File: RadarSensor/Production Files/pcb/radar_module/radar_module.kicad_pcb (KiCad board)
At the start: 2 copper layers, 50 x 25 mm, 14 parts, among them J1 110990030, J3 Conn_01x05_Pin, J4 Conn_02x04_Odd_Even, U1 MIC2288YD5-TR

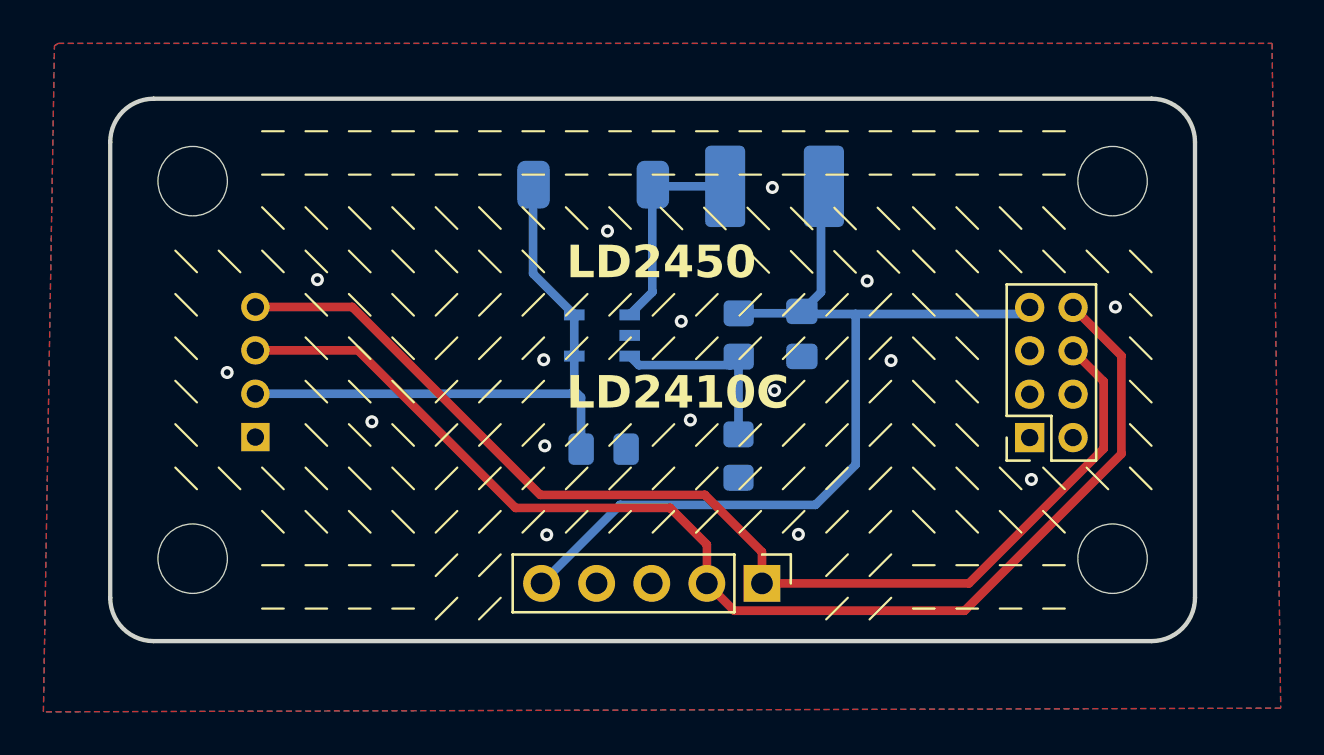
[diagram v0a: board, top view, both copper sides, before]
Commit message: silkscreen for radar sensor, more code examples, better readme
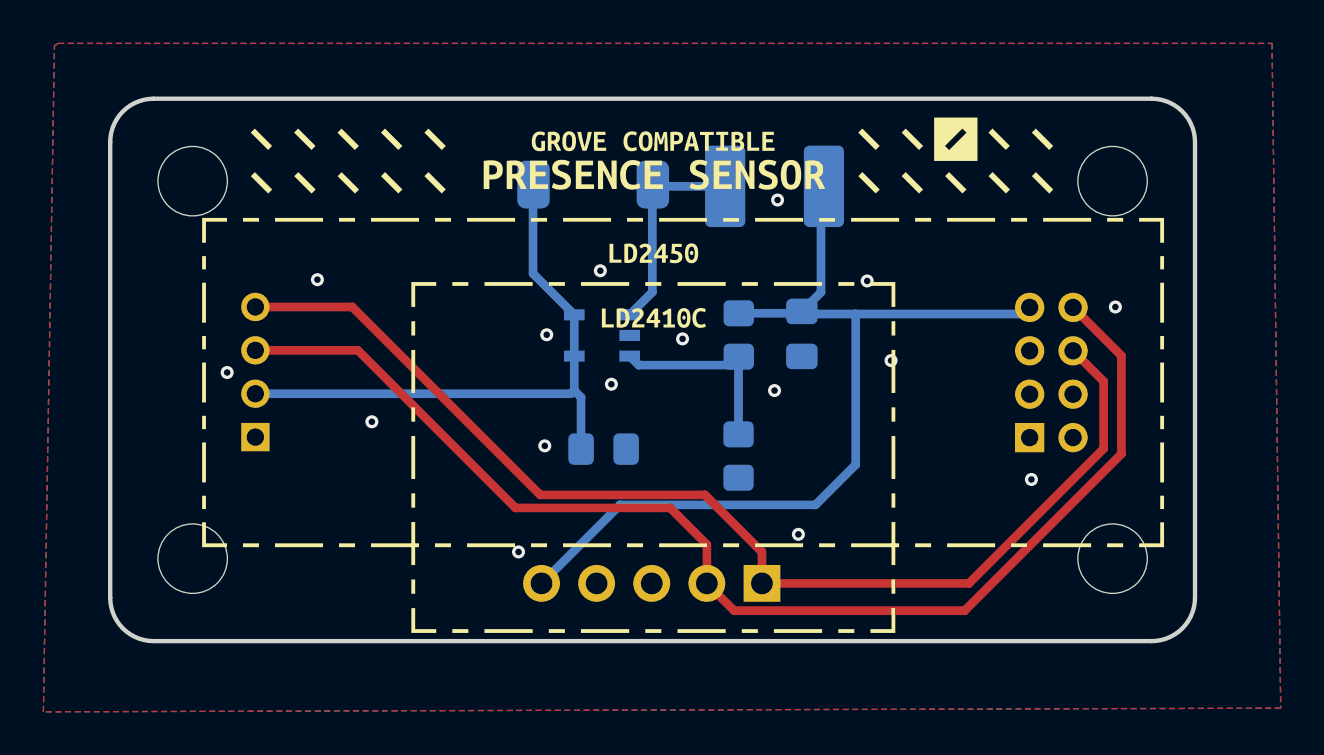
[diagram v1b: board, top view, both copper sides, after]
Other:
- board text removed: "GND"
- board text removed: "LD2410C"
- board text removed: "LD2450"

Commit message: update radar module
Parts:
- J4: moved to B.Cu
- moved J4 5.99 mm to (142.4, 109.6)
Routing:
- net RX: track 56.6 -> 48.7 mm
- net TX: track 52.9 -> 49.7 mm
